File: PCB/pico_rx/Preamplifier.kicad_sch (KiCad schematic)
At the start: 11 parts, among them J5 Antenna, U6 LTC6226xS8

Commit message: Prepare PCB for manufacture
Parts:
- removed C?: 100p, Capacitor_SMD:C_0805_2012Metric, symbol Device:C
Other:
- note added: "WITH PREAMP WITHOUT PREAMP R12 no fit 0 ohm link R1 50 no fit R11 500 0 ohm link C5 10p no fit U6 fit no fit"
- note removed: "R1, C4 determine LPF cutoff 1/(2 * pi * 50 * 100e-12) ~= 30MHz"
- note removed: "WITH PREAMP WITHOUT PREAMP R12 no fit 0 ohm link R1 50 no fit R11 500 0 ohm link C5 10p no fit C4 100p no fit U6 fit no fit"
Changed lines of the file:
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@@
   (junction (at 140.97 96.52) (diameter 0) (color 0 0 0 0)
   )
-  (junction (at 130.81 101.6) (diameter 0) (color 0 0 0 0)
-  )
   (junction (at 190.5 99.06) (diameter 0) (color 0 0 0 0)
   )
@@
     (stroke (width 0) (type default))
   )
-  (wire (pts (xy 130.81 101.6) (xy 130.81 104.14))
-    (stroke (width 0) (type default))
-  )
   (wire (pts (xy 134.62 71.12) (xy 134.62 73.66))
     (stroke (width 0) (type default))
@@
     (stroke (width 0) (type default))
   )
-  (wire (pts (xy 130.81 111.76) (xy 130.81 116.84))
-    (stroke (width 0) (type default))
-  )
   (wire (pts (xy 120.65 96.52) (xy 119.38 96.52))
     (stroke (width 0) (type default))
@@
     (stroke (width 0) (type default))
   )
-  (wire (pts (xy 128.27 101.6) (xy 130.81 101.6))
-    (stroke (width 0) (type default))
-  )
   (wire (pts (xy 161.29 69.85) (xy 151.13 69.85))
     (stroke (width 0) (type default))
@@
     (stroke (width 0) (type default))
   )
-  (wire (pts (xy 130.81 101.6) (xy 147.32 101.6))
+  (wire (pts (xy 128.27 101.6) (xy 147.32 101.6))
     (stroke (width 0) (type default))
   )
@@
   (wire (pts (xy 128.27 96.52) (xy 140.97 96.52))
     (stroke (width 0) (type default))
-  )
-  (text "R1, C4  determine LPF cutoff\n1/(2 * pi * 50 * 100e-12) ~= 30MHz"
-    (at 97.79 138.43 0)
-    (effects (font (size 2.5 2.5)) (justify left bottom))
   )
   (text "no fit" (at 121.92 88.9 0)
@@
     (effects (font (size 2.5 2.5)) (justify left bottom))
   )
-  (text "		WITH PREAMP         WITHOUT PREAMP\n\nR12     no fit              0 ohm link\nR1      50                  no fit\nR11     500                 0 ohm link\nC5      10p                 no fit               \nC4      100p                no fit\nU6      fit                 no fit"
+  (text "		WITH PREAMP         WITHOUT PREAMP\n\nR12     no fit              0 ohm link\nR1      50                  no fit\nR11     500                 0 ohm link\nC5      10p                 no fit               \nU6      fit                 no fit"
     (at 12.7 52.07 0)
     (effects (font (face "FreeMono") (size 3 3) (thickness 0.254) bold) (justify left bottom))
@@
     )
   )
-  (symbol (lib_id "power:GND") (at 130.81 116.84 0) (unit 1)
+  (symbol (lib_id "power:GND") (at 134.62 86.36 0) (unit 1)
     (in_bom yes) (on_board yes) (dnp no)
-    (property "Reference" "#PWR036" (at 130.81 123.19 0)
-      (effects (font (size 1.27 1.27)) hide)
-    )
-    (property "Value" "GND" (at 130.937 121.2342 0)
-      (effects (font (size 1.27 1.27)))
-    )
-    (property "Footprint" "" (at 130.81 116.84 0)
-      (effects (font (size 1.27 1.27)) hide)
-    )
-    (property "Datasheet" "" (at 130.81 116.84 0)
+    (property "Reference" "#PWR036" (at 134.62 92.71 0)
+      (effects (font (size 1.27 1.27)) hide)
+    )
+    (property "Value" "GND" (at 134.747 90.7542 0)
+      (effects (font (size 1.27 1.27)))
+    )
+    (property "Footprint" "" (at 134.62 86.36 0)
+      (effects (font (size 1.27 1.27)) hide)
+    )
+    (property "Datasheet" "" (at 134.62 86.36 0)
       (effects (font (size 1.27 1.27)) hide)
     )
@@
         )
         (path "/b6f73a49-ac1f-4895-a0f9-8f6954ee587f/922c32e5-68dc-43db-b1ed-78e4b25ea173"
-          (reference "#PWR037") (unit 1)
-        )
-      )
-    )
-  )
-  (symbol (lib_id "power:GND") (at 134.62 86.36 0) (unit 1)
-    (in_bom yes) (on_board yes) (dnp no)
-    (property "Reference" "#PWR036" (at 134.62 92.71 0)
-      (effects (font (size 1.27 1.27)) hide)
-    )
-    (property "Value" "GND" (at 134.747 90.7542 0)
-      (effects (font (size 1.27 1.27)))
-    )
-    (property "Footprint" "" (at 134.62 86.36 0)
-      (effects (font (size 1.27 1.27)) hide)
-    )
-    (property "Datasheet" "" (at 134.62 86.36 0)
-      (effects (font (size 1.27 1.27)) hide)
-    )
-    (pin "1")
-    (instances
-      (project "RADIO"
-        (path "/5d930522-554c-4aa3-9994-0a3918a0f6b7/00000000-0000-0000-0000-00005e371e22"
-          (reference "#PWR036") (unit 1)
-        )
-      )
-      (project "pico_rx"
-        (path "/b6f73a49-ac1f-4895-a0f9-8f6954ee587f/2ef3a865-c67c-430c-957b-3defd66f2291"
-          (reference "#PWR034") (unit 1)
-        )
-        (path "/b6f73a49-ac1f-4895-a0f9-8f6954ee587f/b8fbcf71-8210-4060-b465-236d1aa4e7b3"
           (reference "#PWR033") (unit 1)
         )
-        (path "/b6f73a49-ac1f-4895-a0f9-8f6954ee587f/922c32e5-68dc-43db-b1ed-78e4b25ea173"
-          (reference "#PWR033") (unit 1)
-        )
-      )
-    )
-  )
-  (symbol (lib_id "Device:C") (at 130.81 107.95 0) (mirror y) (unit 1)
-    (in_bom yes) (on_board yes) (dnp no)
-    (property "Reference" "C?" (at 137.1346 106.68 0)
-      (effects (font (size 1.27 1.27)))
-    )
-    (property "Value" "100p" (at 137.16 109.22 0)
-      (effects (font (size 1.27 1.27)))
-    )
-    (property "Footprint" "Capacitor_SMD:C_0805_2012Metric" (at 129.8448 111.76 0)
-      (effects (font (size 1.27 1.27)) hide)
-    )
-    (property "Datasheet" "~" (at 130.81 107.95 0)
-      (effects (font (size 1.27 1.27)) hide)
-    )
-    (pin "1")
-    (pin "2")
-    (instances
-      (project "RADIO"
-        (path "/852d5a42-8663-46cd-bbc7-538bfe8c017d/00000000-0000-0000-0000-00005e421de9"
-          (reference "C?") (unit 1)
-        )
-      )
-      (project "pico_rx"
-        (path "/b6f73a49-ac1f-4895-a0f9-8f6954ee587f/b8fbcf71-8210-4060-b465-236d1aa4e7b3"
-          (reference "C1") (unit 1)
-        )
-        (path "/b6f73a49-ac1f-4895-a0f9-8f6954ee587f/922c32e5-68dc-43db-b1ed-78e4b25ea173"
-          (reference "C4") (unit 1)
-        )
-      )
+      )

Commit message: Add gerbers
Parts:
- J5: footprint Connector_Coaxial:SMA_Amphenol_132289_EdgeMount -> Connector_Coaxial:SMA_Samtec_SMA-J-P-X-ST-EM1_EdgeMount
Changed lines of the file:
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@@
       (effects (font (size 1.27 1.27)) (justify left))
     )
-    (property "Footprint" "Connector_Coaxial:SMA_Amphenol_132289_EdgeMount" (at 101.6 101.6 0)
+    (property "Footprint" "Connector_Coaxial:SMA_Samtec_SMA-J-P-X-ST-EM1_EdgeMount" (at 101.6 101.6 0)
       (effects (font (size 1.27 1.27)) hide)
     )

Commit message: Update power calculation
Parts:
- C?: value 10p -> 22p
- R11: value 500 -> 220
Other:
- note added: "R1, R11 determine gain 220/47 = 5x gain 20*log10(220/47) = 13dB gain"
- note added: "R11, C5 determine LPF cutoff 1/(2 * pi * 220 * 22e-12) ~= 30MHz"
- note added: "WITH PREAMP WITHOUT PREAMP R12 no fit 0 ohm link R1 47 no fit R11 220 0 ohm link C5 22p no fit U6 fit no fit"
- note removed: "R1, R11 determine gain 500/50 = 10x gain 20*log10(500/50) = 20dB gain"
- note removed: "R11, C5 determine LPF cutoff 1/(2 * pi * 500 * 10e-12) ~= 30MHz"
- note removed: "WITH PREAMP WITHOUT PREAMP R12 no fit 0 ohm link R1 50 no fit R11 500 0 ohm link C5 10p no fit U6 fit no fit"
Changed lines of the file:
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@@
     (effects (font (size 1.27 1.27)) (justify left bottom))
   )
-  (text "R11, C5  determine LPF cutoff\n1/(2 * pi * 500 * 10e-12) ~= 30MHz"
+  (text "R11, C5  determine LPF cutoff\n1/(2 * pi * 220 * 22e-12) ~= 30MHz"
     (at 154.94 57.15 0)
     (effects (font (size 2.5 2.5)) (justify left bottom))
   )
-  (text "		WITH PREAMP         WITHOUT PREAMP\n\nR12     no fit              0 ohm link\nR1      50                  no fit\nR11     500                 0 ohm link\nC5      10p                 no fit               \nU6      fit                 no fit"
+  (text "		WITH PREAMP         WITHOUT PREAMP\n\nR12     no fit              0 ohm link\nR1      47                  no fit\nR11     220                 0 ohm link\nC5      22p                 no fit               \nU6      fit                 no fit"
     (at 12.7 52.07 0)
     (effects (font (face "FreeMono") (size 3 3) (thickness 0.254) bold) (justify left bottom))
   )
-  (text "R1, R11  determine gain\n500/50 = 10x gain\n20*log10(500/50) = 20dB gain"
+  (text "R1, R11  determine gain\n220/47 = 5x gain\n20*log10(220/47) = 13dB gain"
     (at 204.47 81.28 0)
     (effects (font (size 2.5 2.5)) (justify left bottom))
@@
       (effects (font (size 1.27 1.27)))
     )
-    (property "Value" "10p" (at 166.37 63.5 0)
+    (property "Value" "22p" (at 166.37 63.5 0)
       (effects (font (size 1.27 1.27)))
     )
@@
       (effects (font (size 1.27 1.27)) (justify left))
     )
-    (property "Value" "500" (at 166.243 78.232 0)
-      (effects (font (size 1.27 1.27)) (justify left))
-    )
+    (property "Value" "220" (at 166.243 78.232 0)
+      (effects (font (size 1.27 1.27)) (justify left))
+    )

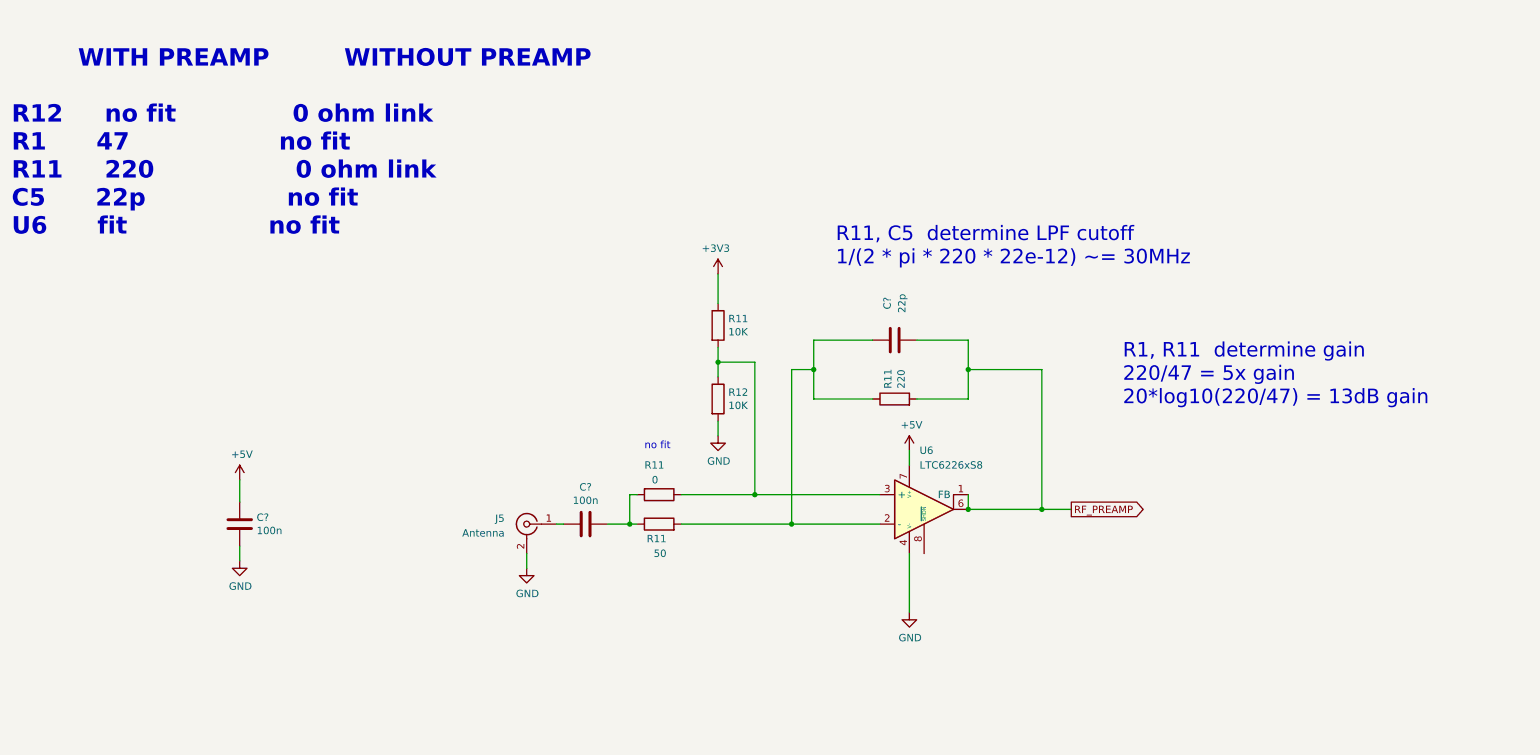
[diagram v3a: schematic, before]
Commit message: Improve frequency resolution by making small adjustments to system clock. Add utility to upload memory contents over USB
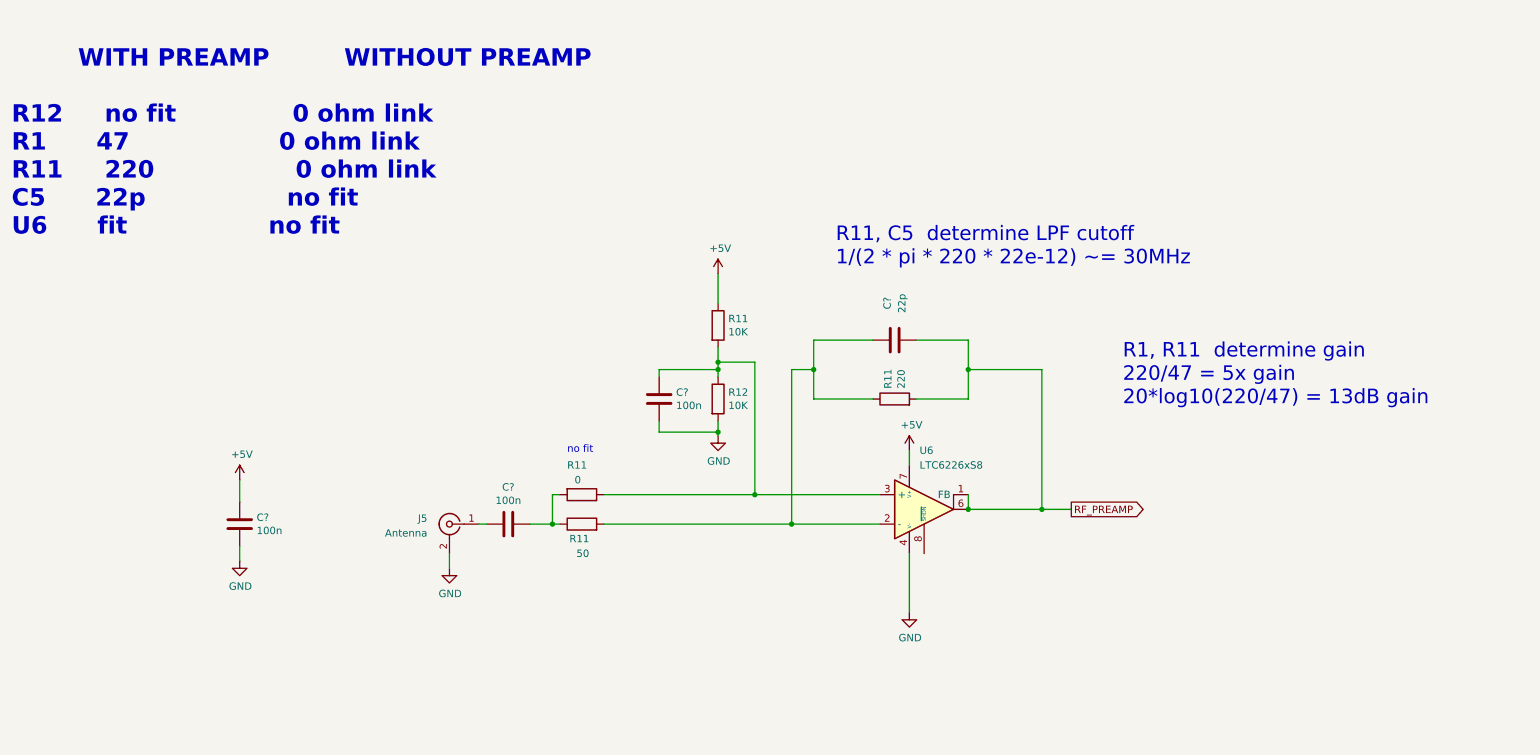
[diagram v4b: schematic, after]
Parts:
- added C?: 100n, Capacitor_SMD:C_0805_2012Metric, symbol Device:C
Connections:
- net +3V3 is gone; now on net +5V: R11.1
- net GND: now also C?.2
- net at R11.1, R11.2, R12.1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: now also C?.1
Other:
- note added: "WITH PREAMP WITHOUT PREAMP R12 no fit 0 ohm link R1 47 0 ohm link R11 220 0 ohm link C5 22p no fit U6 fit no fit"
- note removed: "WITH PREAMP WITHOUT PREAMP R12 no fit 0 ohm link R1 47 no fit R11 220 0 ohm link C5 22p no fit U6 fit no fit"
- moved on the sheet: C?, J5, R11

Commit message: Update PCB design to fix issues found
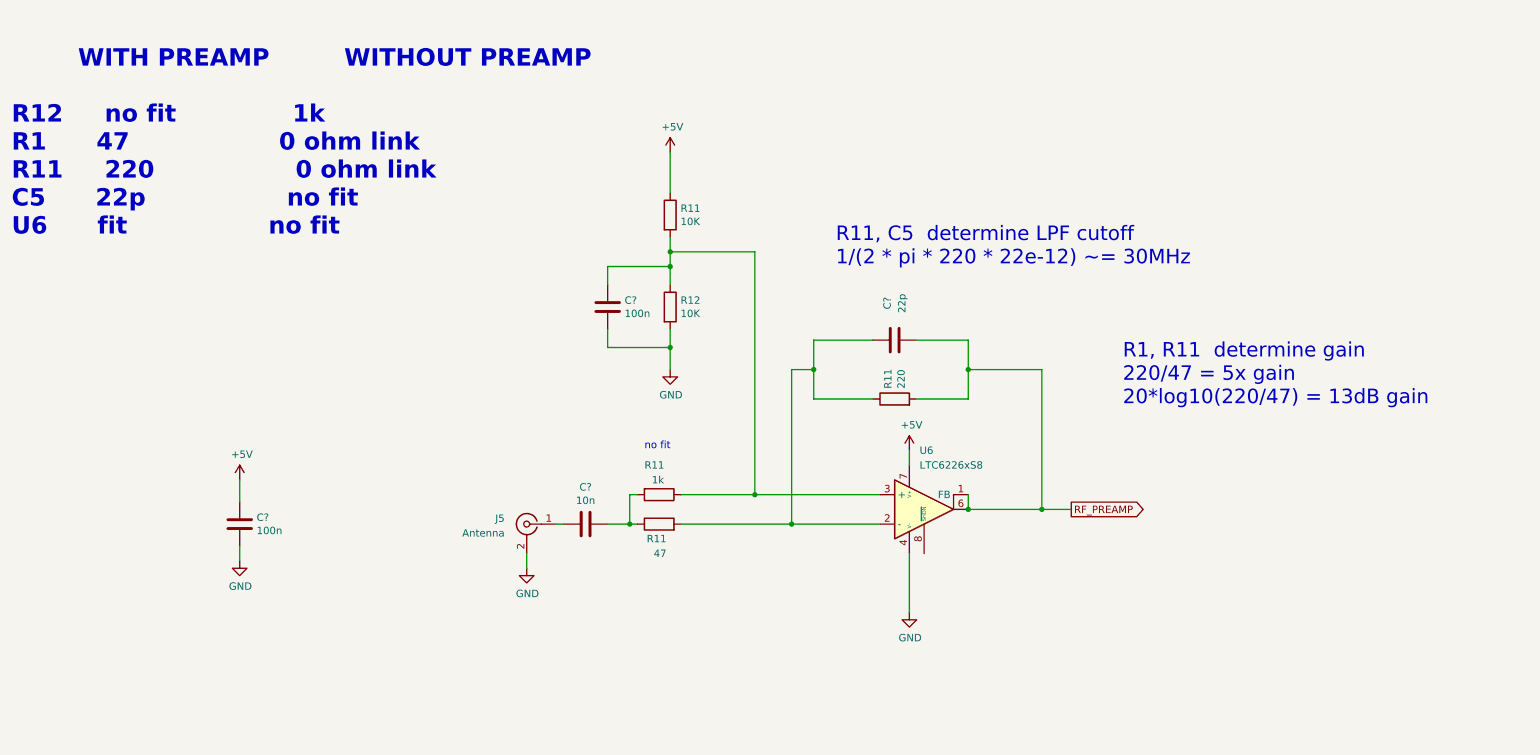
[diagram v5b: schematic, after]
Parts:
- removed C?: 100n, Capacitor_SMD:C_0805_2012Metric, symbol Device:C
- added C?: 100n, Capacitor_SMD:C_0805_2012Metric, symbol Device:C
- C?: value 100n -> 10n
- R11: value 0 -> 1k
- R11: value 50 -> 47
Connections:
- net GND: now also C?.2
- net at R11.1, R11.2, R12.1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: now also C?.1
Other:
- note added: "WITH PREAMP WITHOUT PREAMP R12 no fit 1k R1 47 0 ohm link R11 220 0 ohm link C5 22p no fit U6 fit no fit"
- note removed: "WITH PREAMP WITHOUT PREAMP R12 no fit 0 ohm link R1 47 0 ohm link R11 220 0 ohm link C5 22p no fit U6 fit no fit"
- moved on the sheet: C?, J5, R11, R12
